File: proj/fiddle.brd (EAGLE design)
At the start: 44.1 x 15.2 mm, 12 parts, among them SW6 TACTSW_2MICRO3X6, SW7 TACTSW_2MICRO3X6, U1 MCP23008QFN, U4 3.3V

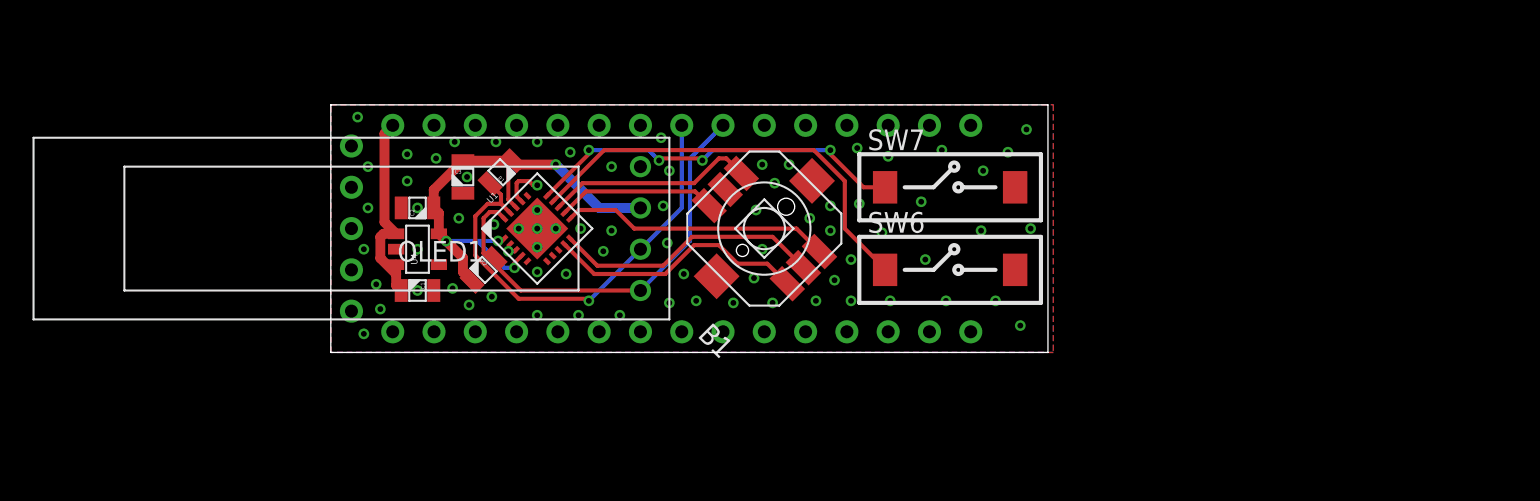
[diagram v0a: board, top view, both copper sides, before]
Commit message: Moved 0.91 OLED footprint to docu layer Updated Fiddle schematic & board to include MicroSD and Wifi (esp8266) :D
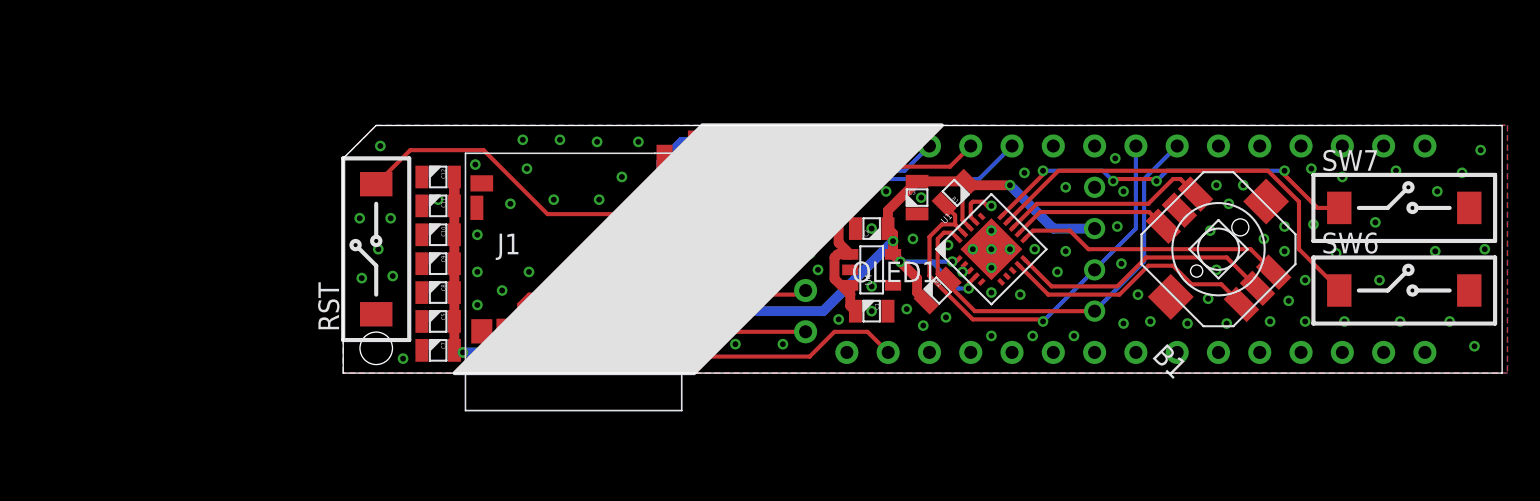
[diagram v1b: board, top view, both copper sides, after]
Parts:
- added C10, C11, C12, C4, C5, C8, C9: 10uF, dooba:0805
- added C6, C7: 100nF, dooba:0805
- added J1: DM3D-SFDM, dooba:DM3D-SF
- added RST: TACTSW_2MICRO3X6, dooba:TACTSW_MICRO3X6
- added U2: WRL-13678WRL-13678-QUIET, dooba:WRL-13678-QUIET
- U4: value 3.3V -> 3.3V 600mA
- moved N1 28.0 mm to (66.0, 40.6)
- moved C1 28.0 mm to (48.5, 36.8)
- moved C2 28.0 mm to (48.5, 41.9)
- moved C3 28.0 mm to (51.3, 43.8)
- moved OLED1 28.0 mm to (44.5, 40.6)
- moved R2 28.0 mm to (52.6, 38.1)
- moved U1 28.0 mm to (55.9, 40.6)
- moved U4 28.0 mm to (48.5, 39.4)
- moved B1 28.0 mm to (69.8, 40.6)
- moved R1 28.0 mm to (53.7, 44.1)
- moved SW6 28.0 mm to (81.3, 38.1)
- moved SW7 28.0 mm to (81.3, 43.2)
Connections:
- new net MICROSD_CS: J1.DAT3/CS, N1.14
- new net N$8: N1.34, RST.2
- new net SPI_MISO: J1.DAT0/DO, N1.32
- new net SPI_MOSI: J1.CMD/DI, N1.31
- new net SPI_SCK: J1.CLK/SCK, N1.33
- new net WIFI_FLASH: N1.20, U2.5
- new net WIFI_RST: N1.19, U2.6
- new net WIFI_RX: N1.17, U2.2
- new net WIFI_TX: N1.18, U2.7
- net 3.3V: now also C10.1, C11.1, C12.1, C4.1, C5.1, C6.1, C7.1, C8.1, C9.1, J1.VDD, U2.4, U2.8
- net GND: now also C10.2, C11.2, C12.2, C4.2, C5.2, C6.2, C7.2, C8.2, C9.2, J1.GND1, J1.GND2, J1.GND3, J1.GND4, J1.VSS, RST.1, U2.1
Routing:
- net 3.3V: track 32.0 -> 99.9 mm, vias 4 -> 9
- net N$8: track 0.00 -> 29.1 mm
- net WIFI_TX: track 0.00 -> 22.8 mm
- net WIFI_FLASH: track 0.00 -> 22.2 mm, vias 0 -> 1
- net SPI_MISO: track 0.00 -> 19.7 mm
- net MICROSD_CS: track 0.00 -> 19.6 mm
- net SPI_SCK: track 0.00 -> 18.6 mm, vias 0 -> 2
- net WIFI_RST: track 0.00 -> 17.3 mm, vias 0 -> 2
- net SPI_MOSI: track 0.00 -> 15.4 mm
- net WIFI_RX: track 0.00 -> 11.0 mm
- net GND: vias 77 -> 110
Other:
- board size 44.1 x 15.2 mm -> 71.3 x 15.2 mm

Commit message: tootoot
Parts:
- added P1, P2: PIN_8, dooba:PIN_8
- added P3, P4: PIN_4, dooba:PIN_4
- added P5: PIN_2, dooba:PIN_2
- added P6: PIN_3, dooba:PIN_3
- added P7: PIN_1, dooba:PIN_1
- moved C10 21.7 mm to (41.8, 33.0), turned to 270 degrees
- moved C11 20.9 mm to (40.0, 33.0), turned to 270 degrees
- moved C12 20.3 mm to (38.2, 33.0), turned to 270 degrees
- moved RST 15.1 mm to (30.7, 48.8), turned to 0 degrees
- moved C9 5.50 mm to (22.5, 45.2), turned to 270 degrees
- moved C8 3.49 mm to (22.5, 41.4), turned to 270 degrees
- moved C6 3.30 mm to (38.6, 47.2), turned to 180 degrees
- moved C4 2.03 mm to (38.6, 49.3)
- moved C5 1.53 mm to (22.5, 37.6), turned to 270 degrees
- moved C1 1.27 mm to (48.5, 38.1)
- moved C2 1.27 mm to (48.5, 43.2)
- moved U4 1.27 mm to (48.5, 40.6)
- moved C7 0.90 mm to (22.5, 33.8), turned to 270 degrees
- moved J1 0.51 mm to (30.2, 36.3)
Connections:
- removed net 5.5V: C1.2, N1.16, U4.1, U4.3
- new net N$10: N1.29, P2.7
- new net N$11: N1.28, P2.6
- new net N$12: N1.27, P2.5
- new net N$13: N1.26, P2.4
- new net N$14: N1.25, P2.3
- new net N$15: N1.3, P1.8
- new net N$16: N1.4, P1.7
- new net N$17: N1.5, P1.6
- new net N$18: N1.6, P1.5
- new net N$19: N1.7, P1.4
- new net N$20: N1.8, P1.3
- new net N$21: N1.9, P1.2
- new net N$22: N1.10, P1.1
- new net N$23: N1.22, P4.4
- new net N$24: N1.21, P4.3
- new net N$25: N1.20, P4.2
- new net N$26: N1.19, P4.1
- new net N$27: N1.14, P7.1
- new net N$9: N1.30, P2.8
- new net VIN: C1.2, N1.16, P6.2, U4.1, U4.3
- new net VUSB: N1.2, P5.2
- net 3.3V: now also P6.3
- net GND: now also P5.1, P6.1
- net I2C_SCL: now also P2.1
- net I2C_SDA: now also P2.2
- net MICROSD_CS: now also N1.13; no longer N1.14
- net N$8: now also P3.1
- net SPI_MISO: now also P3.3
- net SPI_MOSI: now also P3.2
- net SPI_SCK: now also P3.4
- net WIFI_FLASH: now also N1.11; no longer N1.20
- net WIFI_RST: now also N1.12; no longer N1.19
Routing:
- net VIN: track 0.00 -> 15.7 mm
- net SPI_SCK: track 18.6 -> 34.0 mm
- net 3.3V: track 99.9 -> 114.6 mm, vias 9 -> 13
- net 5.5V: track 12.6 -> 0.00 mm
- net SPI_MISO: track 19.7 -> 31.4 mm
- net GND: track 3.38 -> 13.3 mm, vias 110 -> 107
- net N$27: track 0.00 -> 8.67 mm
- net SPI_MOSI: track 15.4 -> 23.3 mm, vias 0 -> 1
- net WIFI_RST: track 17.3 -> 21.9 mm, vias 2 -> 0
- net WIFI_FLASH: track 22.2 -> 26.5 mm, vias 1 -> 0
- net MICROSD_CS: track 19.6 -> 23.4 mm, vias 0 -> 2
- net VUSB: track 0.00 -> 2.54 mm
- net N$9: track 0.00 -> 2.54 mm
- net N$26: track 0.00 -> 2.54 mm
- net N$25: track 0.00 -> 2.54 mm
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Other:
- board size 71.3 x 15.2 mm -> 66.2 x 20.3 mm
